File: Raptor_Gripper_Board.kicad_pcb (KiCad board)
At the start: 2 copper layers, 50.2 x 51.4 mm, 14 parts, among them J1 Conn_01x02, J2 Conn_01x03, J3 Conn_01x03, J4 Conn_01x03, J5 Conn_01x03

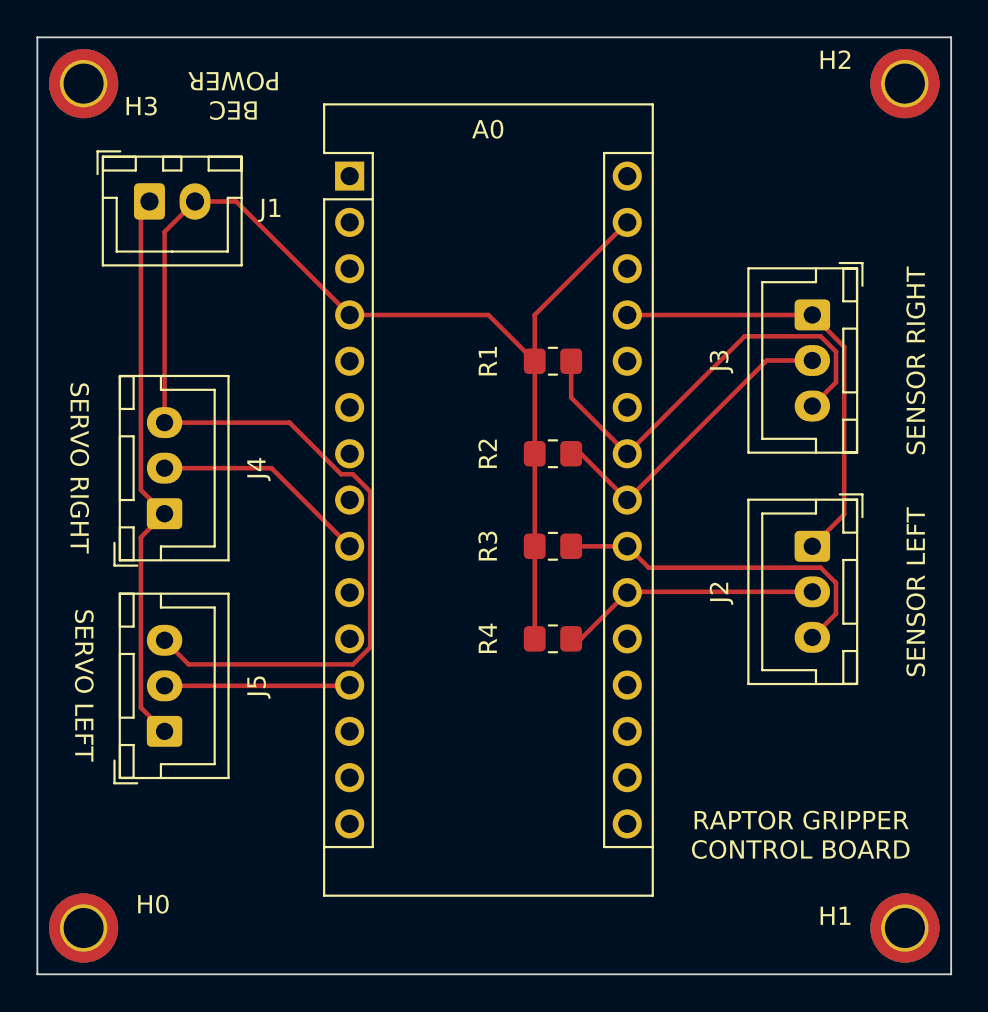
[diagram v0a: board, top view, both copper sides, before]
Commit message: added support for third servo
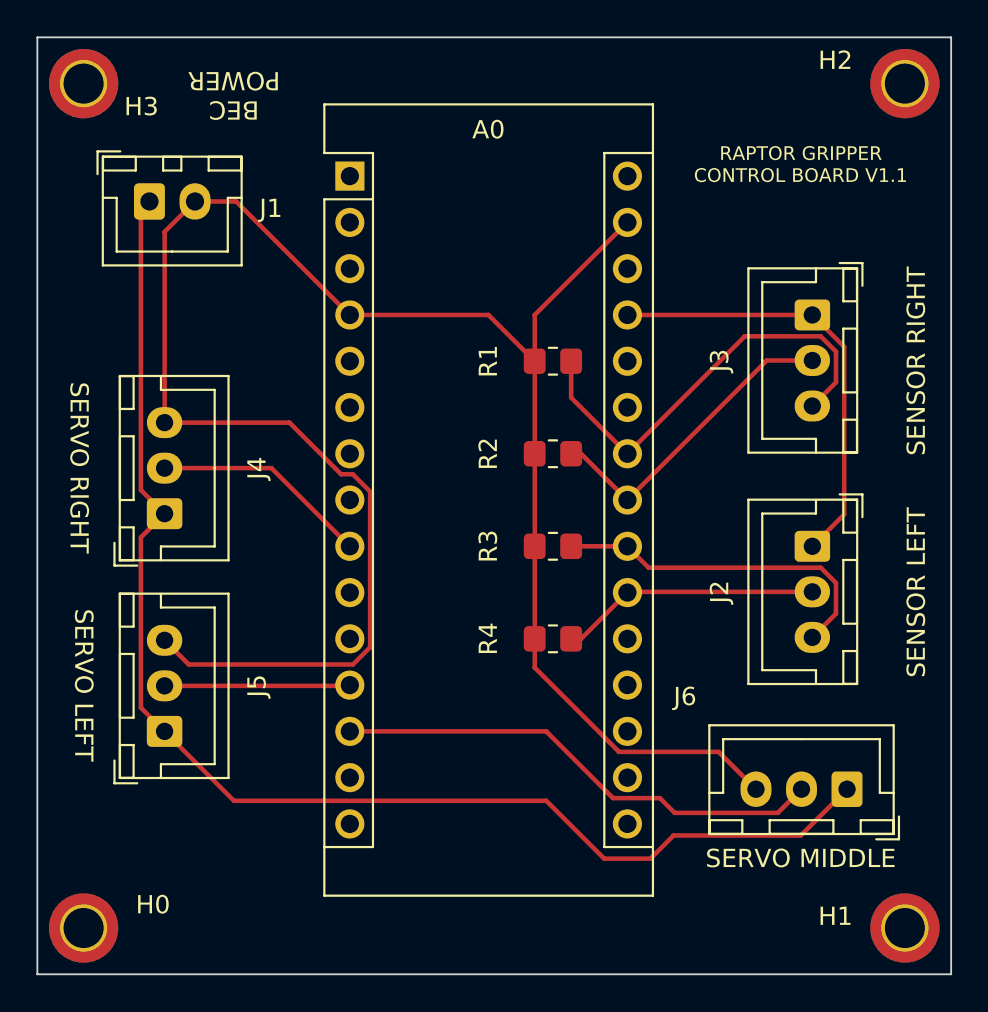
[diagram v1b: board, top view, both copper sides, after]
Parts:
- added J6: Conn_01x03, Connector_JST:JST_XH_B3B-XH-A_1x03_P2.50mm_Vertical, F.Cu at (121.3, 84.5)
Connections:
- A0 pad 13: unconnected-(A0-Pad13) -> Net-(A0-Pad13)
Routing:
- net Net-(J1-Pad1): track 30.9 -> 72.8 mm
- net Net-(A0-Pad13): track 0.00 -> 27.2 mm
- net Net-(A0-Pad29): track 93.7 -> 110.2 mm
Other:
- board text added: "RAPTOR GRIPPER CONTROL BOARD V1.1"
- board text added: "SERVO MIDDLE"
- board text removed: "RAPTOR GRIPPER CONTROL BOARD"
